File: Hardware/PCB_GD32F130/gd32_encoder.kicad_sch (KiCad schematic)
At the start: 26 parts, among them J1 Conn_01x03_Pin, J2 Conn_01x03_Pin, J3 Conn_01x04_Pin, Q1 2N7002K, U1 XC6206PxxxMR, U2 MT6701CT, U3 GD32F130F4P6TR

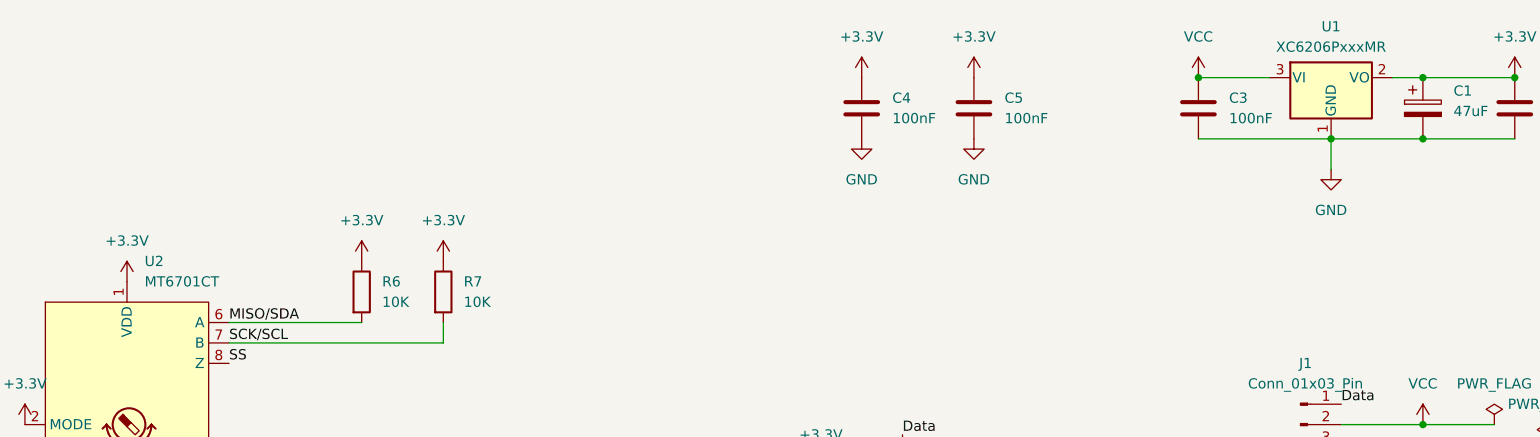
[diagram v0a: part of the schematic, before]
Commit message: Updated 3.3V regulator with HT7533S that supports 12V input. / Mentioned AS5600 compatibility.
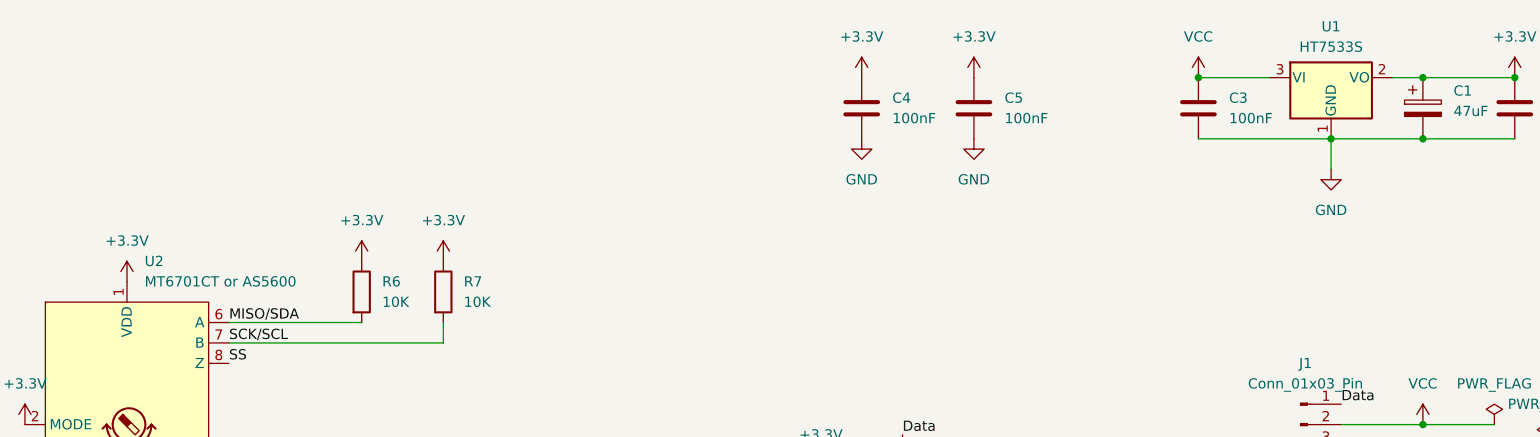
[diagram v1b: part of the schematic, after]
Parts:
- U1: value XC6206PxxxMR -> HT7533S
- U2: value MT6701CT -> MT6701CT or AS5600
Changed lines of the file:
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@@
 			)
 		)
-		(property "Value" "MT6701CT"
+		(property "Value" "MT6701CT or AS5600"
 			(at 93.6341 52.07 0)
 			(effects
@@
 			)
 		)
-		(property "Value" "XC6206PxxxMR"
+		(property "Value" "HT7533S"
 			(at 241.3 22.86 0)
 			(effects

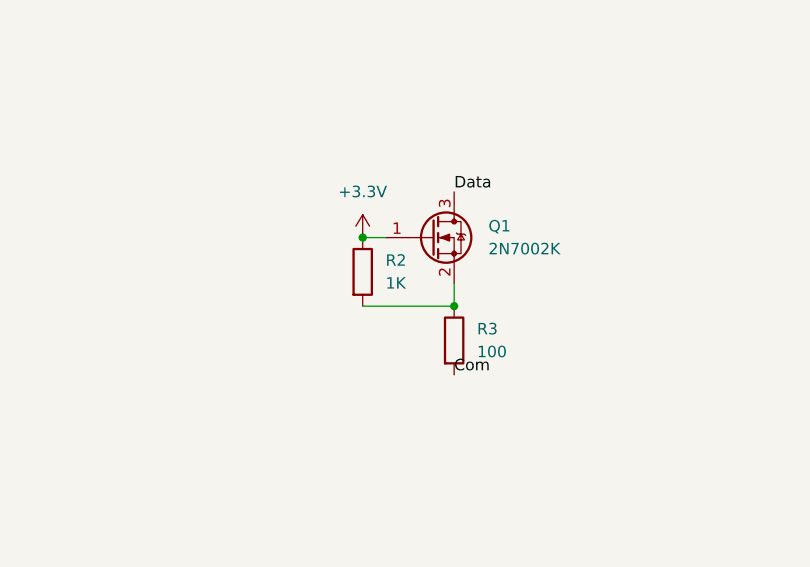
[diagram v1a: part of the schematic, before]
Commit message: Fixed R2 resistor value
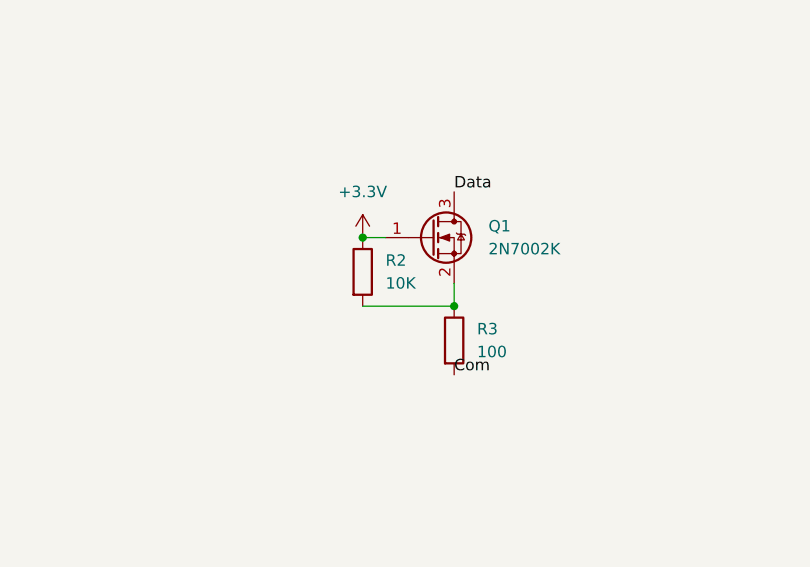
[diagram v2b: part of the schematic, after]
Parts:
- R2: value 1K -> 10K
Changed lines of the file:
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@@
 			)
 		)
-		(property "Value" "1K"
+		(property "Value" "10K"
 			(at 180.34 81.2799 0)
 			(effects
